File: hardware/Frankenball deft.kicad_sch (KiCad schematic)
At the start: 8 parts, among them J51 Conn_02x03_Odd_Even, J52 Conn_01x06, J53 Conn_01x04_Male, J54 Conn_01x12, J55 Conn_01x05_Female, SW51 SW_Push

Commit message: Am I done?
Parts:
- removed J51: Conn_02x03_Odd_Even, symbol Connector_Generic:Conn_02x03_Odd_Even
- added R53: 10k, Resistor_SMD:R_0402_1005Metric, symbol Device:R
- J52: value Conn_01x06 -> PWM3320; footprint Connector_FFC-FPC:Hirose_FH12-6S-0.5SH_1x06-1MP_P0.50mm_Horizontal -> Library:FFC Clamshell 0.5mm 6P; Field4 TODO FOOTPRINT -> (none)
- J54: footprint Connector_FFC-FPC:Hirose_FH12-12S-0.5SH_1x12-1MP_P0.50mm_Horizontal -> Library:FFC Clamshell 0.5mm 12P; Field4 TODO FOotprint -> (none)
- SW51: footprint (none) -> Library:Mouse Microswitch SPDT; symbol Switch:SW_Push -> Switch:SW_SPDT
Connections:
- net PA3 is gone; now on net PA6: J54.9 (Pin_9)
- net PA4 is gone; now on net BTN_{HIST2}: J54.10 (Pin_10)
- net PA7 is gone; now on net PA10: J54.5 (Pin_5)
- net PB8 is gone; now on net PA5: J54.8 (Pin_8)
- net PBu12 is gone; now on net PBu13: J52.6 (Pin_6)
- net PBu15 is gone; now on net INT_{Motion}: J52.5 (Pin_5)
- net +3V3: now also J52.4 (Pin_4), J54.7 (Pin_7); no longer J52.3 (Pin_3), J54.6 (Pin_6)
- net BTN_{HIST1}: now also J54.11 (Pin_11); no longer J54.2 (Pin_2)
- net BTN_{HIST2}: no longer J54.3 (Pin_3)
- net BTN_{LEFT}: now also J54.1 (Pin_1); no longer J54.12 (Pin_12)
- net BTN_{RIGHT}: now also SW51.3 (C); no longer SW51.2
- net GND: now also J52.3 (Pin_3), J54.12 (Pin_12), J55.4 (Pin_4), SW51.2 (B), R53.1; no longer J52.4 (Pin_4), J54.1 (Pin_1), J55.2 (Pin_2), SW51.1
- net INT_{Motion}: no longer J52.2 (Pin_2)
- net LED-: now also J54.6 (Pin_6); no longer J54.7 (Pin_7)
- net PA1: now also J52.1 (Pin_1)
- net PA5: no longer J54.11 (Pin_11)
- net PA6: no longer J54.4 (Pin_4)
- net PBu13: no longer J52.1 (Pin_1)
- net USB_DP: now also J55.2 (Pin_2); no longer J55.4 (Pin_4)
- net USB_SHIELD: now also J55.1 (Pin_1); no longer J55.5 (Pin_5)
- net VCC: now also J55.5 (Pin_5); no longer J55.1 (Pin_1)
- new net PA15: J54.4 (Pin_4)
- new net PB3: J54.3 (Pin_3)
- new net PB4: J54.2 (Pin_2)
- new net ~{CS}: J52.2 (Pin_2), R53.2
- no-connect marks 3 -> 4
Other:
- moved on the sheet: J52, J53, J54, J55, R51, R52

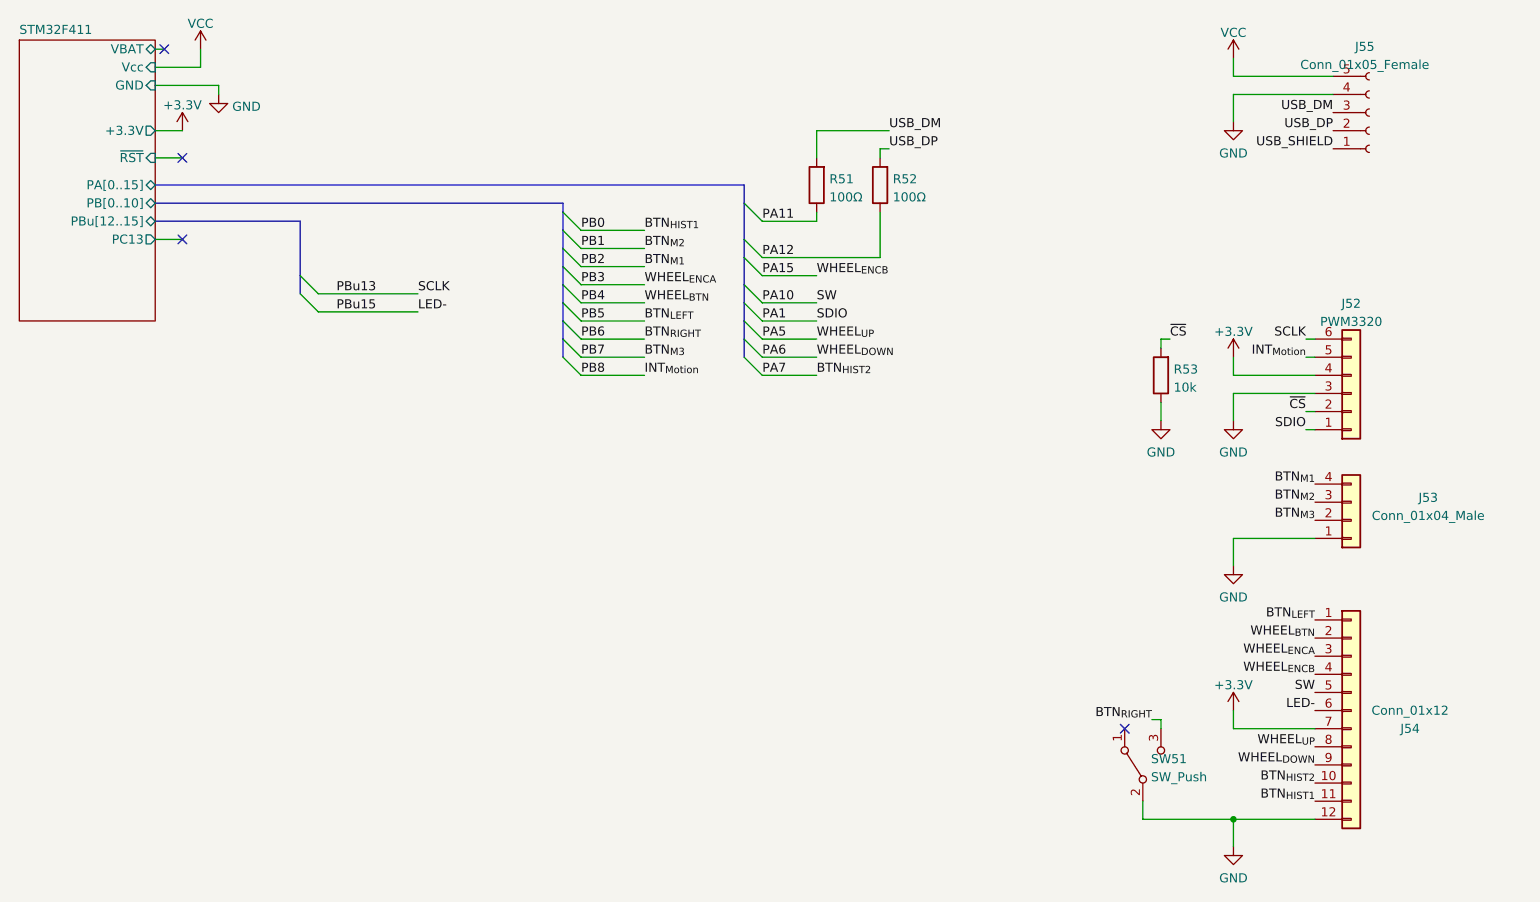
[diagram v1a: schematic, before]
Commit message: Replace boot config header with PFET
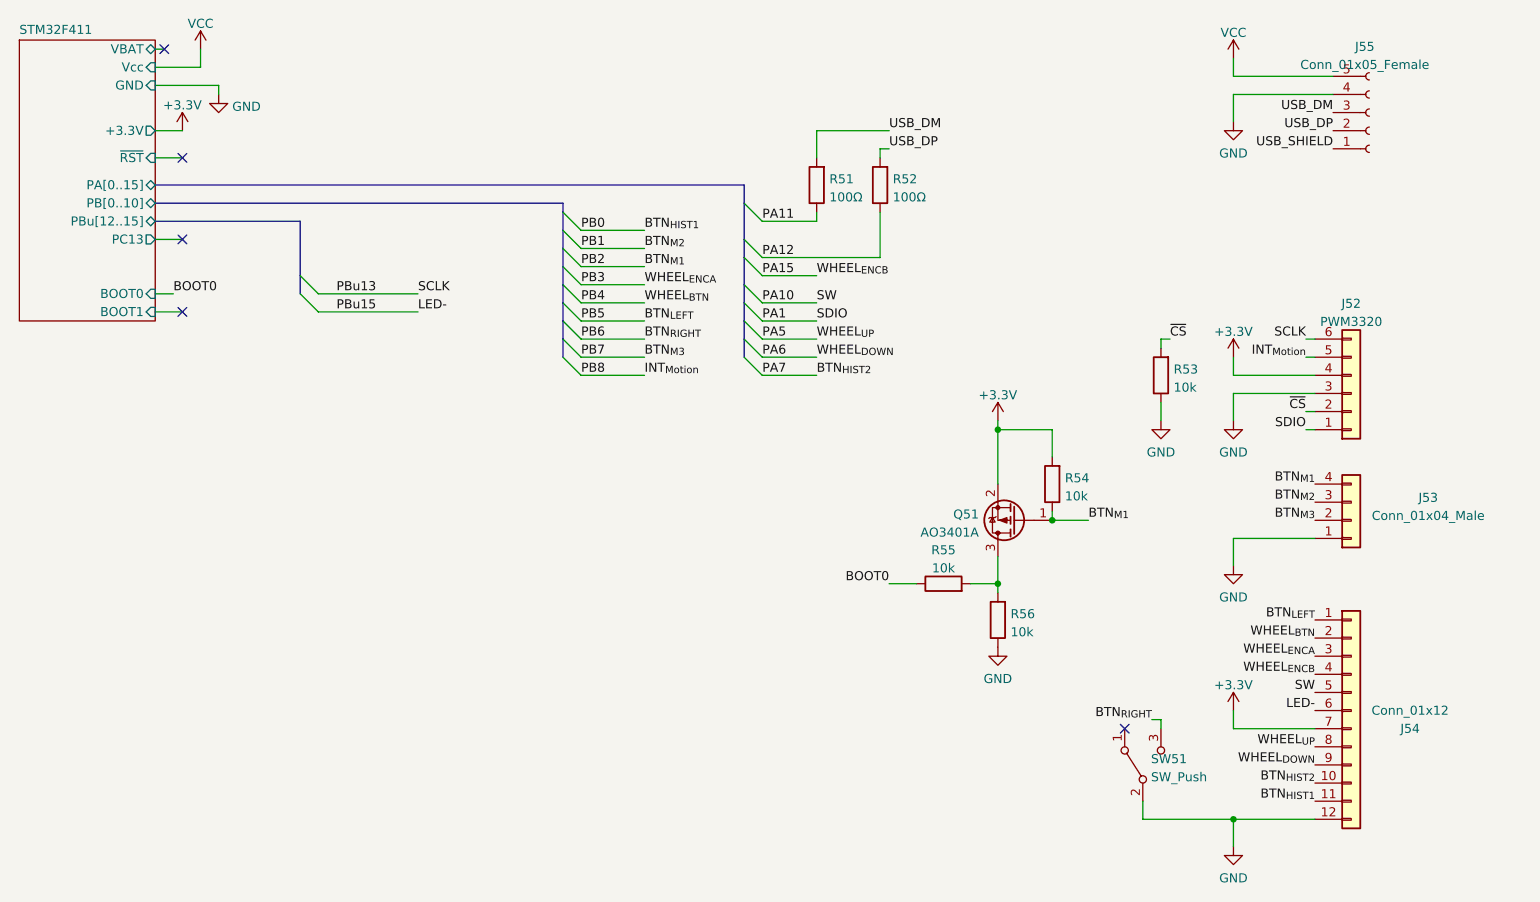
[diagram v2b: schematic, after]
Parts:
- added Q51: AO3401A, Package_TO_SOT_SMD:SOT-23, symbol Device:Q_PMOS_GSD
- added R54, R55, R56: 10k, Resistor_SMD:R_0402_1005Metric, symbol Device:R
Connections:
- net +3V3: now also Q51.2 (S), R54.2
- net BTN_{M1}: now also Q51.1 (G), R54.1
- net GND: now also R56.1
- new net: Q51.3 (D), R55.2, R56.2
- new net BOOT0: R55.1
- no-connect marks 4 -> 5
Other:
- sheet STM32F411 ports: added BOOT0, BOOT1; removed none
